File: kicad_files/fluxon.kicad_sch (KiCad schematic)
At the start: 159 parts, among them J1 Conn_ARM_JTAG_SWD_10, J2 U-F-M5DD-W-2, Q1 DTC123JKAT146, Q2 AO3402, SW1 ESC, SW10 O, SW11 P, SW12 DEL, SW13 BKSP, SW14 TAB_125, SW15 A, SW16 S, SW17 D, SW18 F, SW19 G, SW2 Q, SW20 H, SW21 J, SW22 K, SW23 L, SW24 QUOTE, SW25 ENTER_175, SW26 LSHIFT_175, SW27 Z, SW28 X, SW29 C, SW3 W, SW30 V, SW31 B, SW32 N, SW33 M, SW34 COMMA, SW35 DOT, SW36 RSHIFT_125, SW37 FN_100, SW38 RSHIFT_225, SW39 LCTRL_125, SW4 E, SW40 SUPER_100, SW41 LALT_100, SW42 SPC_625, SW43 RALT_125, SW44 RGUI_100, SW45 RCTRL_125, SW46 PN_100, SW47 SPC_175, SW48 SPC_275, SW49 FN_100, SW5 R, SW50 RALT_100, SW51 LCTRL_150, SW52 LALT_150, SW53 SPC_700, SW54 RCTRL_150, SW55 RALT_150, SW56 SW_Push, SW57 Rotary_Encoder_Switch_Chassis, SW6 T, SW7 Y, SW8 U, SW9 I, U1 USBLC6-2SC6, U2 STM32F072CBT6, U3 MCP1700-3302E/TT

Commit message: Add software reset circuit
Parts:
- removed C10: 4.7nF, Capacitor_SMD:C_0805_2012Metric, symbol Device:C_Small
- removed C11, C12: 100n, Capacitor_SMD:C_0805_2012Metric_Pad1.15x1.40mm_HandSolder, symbol Device:C_Small
- removed R13: 1M, acheron_Components:R_SMD_1206, symbol Device:R_Small
- removed R15, R16, R17, R18: 10k, acheron_Components:R_SMD_1206, symbol Device:R_Small
- removed SW57: Rotary_Encoder_Switch_Chassis, acheron_Hardware:ALPS_EC11E, symbol acheronSymbols:Rotary_Encoder_Switch_Chassis
- added Q3: DTA143EKAT146, Package_TO_SOT_SMD:SOT-23, symbol Transistor_BJT:DTA143E
- added R1: 100, acheron_Components:R_SMD_1206, symbol Device:R_Small
- added SW57: (I) RSHIFT_125, acheron_MX_SolderMask:MX125, symbol acheronSymbols:MXSwitch
- added SW58: BKSP_2U, acheron_MX_SolderMask:MX200, symbol acheronSymbols:MXSwitch
- added SW59: (I) SLASH_100, acheron_MX_SolderMask:MX100, symbol acheronSymbols:MXSwitch
- C10: renamed from CB2; value 100nF -> 100n
- C12: renamed from CB4; value 4.7uF -> 4.7u
- C13: renamed from CB5; value 1uF -> 1u
- C16: renamed from CB8; value 4.7uF -> 4.7u
- SW36: value RSHIFT_125 -> (D) RSHIFT_125
- SW37: value FN_100 -> (D) FN_100
- SW38: value RSHIFT_225 -> (F) RSHIFT_225
- renumbered CB1 to C1, CB3 to C11, CB6 to C14, CB7 to C15
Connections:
- net ROT_A is gone; now on net Col12: U2.42 (I2C1_SCL/PB6)
- net 3.3V: now also Q3.2 (E)
- net BOOT0: now also R1.2
- net Col11: now also SW59.1 (Col)
- net Col12: now also SW57.1 (Col), SW58.2 (Row); no longer U2.40 (SPI1_MISO/I2S1_MCK/TIM3_CH1/PB4)
- net at D36.2 (A), SW36.2 (Row), SW38.2 (Row): now also SW59.2 (Row)
- net at D37.2 (A), SW37.2 (Row): now also SW57.2 (Row)
- net M1: no longer names the net of D13.2 (A), SW13.1 (Col)
- net M1: now also SW58.1 (Col)
- net ROT_B renamed SOFT_RESET
- net SOFT_RESET: now also Q3.1 (B)
- new net: Q3.3 (C), R1.1
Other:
- note added: "(L) "Long" 6.25 bottom row"
- note removed: "(L) 6.25 bottom row"
- moved on the sheet: C2, C4, D49, Q1, R14, R3, R4, SW56

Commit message: Finish routing
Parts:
- removed Q1: DTC123JKAT146, Package_TO_SOT_SMD:SOT-23, symbol Transistor_BJT:DTC123J
- removed Q3: DTA143EKAT146, Package_TO_SOT_SMD:SOT-23, symbol Transistor_BJT:DTA143E
- added GR6: Warning Sign, acheron_Graphics:warning_sign_3.6x3.2mm, symbol Mechanical:MountingHole
- added J3: Conn_02x10, acheron_Connectors:PinHeader_2x8_P2.54mm_Vertical, symbol Connector_Generic:Conn_01x16
- added Q2: MUN5335DW1T1G, acheron_Components:SOT-363_SC-70-6, symbol acheronSymbols:MUN5335DW1T1G
- R8: renamed from R5; value 100K -> 100k
- R9: renamed from R6; value 100K -> 100k
- renumbered C9 to C1, C7 to C2, C8 to C3, C3 to C4, C2 to C7, C4 to C8, C1 to C9, D14 to D13, D15 to D14, D16 to D15, D17 to D16, D18 to D17, D19 to D18, D20 to D19, D21 to D20, D22 to D21, D23 to D22, D24 to D23, D25 to D24, D26 to D25, D27 to D26, D28 to D27, D29 to D28, D30 to D29, D31 to D30, D32 to D31, D33 to D32, D34 to D33, D35 to D34, D36 to D35, D37 to D36, D38 to D37, D39 to D38, D40 to D39, D41 to D40, D42 to D41, D43 to D42, D44 to D43, D13 to D44, D52 to D48, D53 to D49, D54 to D50, D50 to D51, D51 to D52, D49 to D53, Q2 to Q1, R9 to R1, R14 to R10, R1 to R11, R3 to R12, R4 to R13, R7 to R2, R8 to R3, R10 to R4, R11 to R5, R12 to R6, R2 to R7, SW14 to SW13, SW15 to SW14, SW16 to SW15, SW17 to SW16, SW18 to SW17, SW19 to SW18, SW20 to SW19, SW21 to SW20, SW22 to SW21, SW23 to SW22, SW24 to SW23, SW25 to SW24, SW26 to SW25, SW27 to SW26, SW28 to SW27, SW29 to SW28, SW30 to SW29, SW31 to SW30, SW32 to SW31, SW33 to SW32, SW34 to SW33, SW35 to SW34, SW36 to SW35, SW37 to SW36, SW38 to SW37, SW57 to SW38, SW59 to SW39, SW39 to SW40, SW40 to SW41, SW41 to SW42, SW42 to SW43, SW43 to SW44, SW44 to SW45, SW45 to SW46, SW13 to SW47, SW58 to SW48, SW46 to SW49, SW47 to SW50, SW48 to SW51, SW49 to SW52, SW50 to SW53, SW51 to SW54, SW52 to SW55, SW53 to SW56, SW54 to SW57, SW55 to SW58, SW56 to SW59, U3 to U2, U2 to U3
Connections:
- net 3.3V: now also J3.15 (Pin_15), Q2.4 (C)
- net 5V: now also R2.1; no longer R2.2
- net Col1: now also U3.25 (PB12)
- net Col12: now also U3.41 (SPI1_MOSI/I2S1_SD/TIM3_CH2/PB5); no longer U3.42 (I2C1_SCL/PB6)
- net GND: now also J3.16 (Pin_16), Q2.1 (C)
- net Row1: now also U3.38 (PA15)
- net Row2: now also U3.39 (SPI1_SCK/I2S1_CK/TIM2_CH2/PB3)
- net Row4: now also U3.42 (I2C1_SCL/PB6)
- net SOFT_RESET: now also U3.40 (SPI1_MISO/I2S1_MCK/TIM3_CH1/PB4), Q2.5 (B); no longer U3.41 (SPI1_MOSI/I2S1_SD/TIM3_CH2/PB5)
- net at D53.2 (A), SW59.2: now also Q2.2 (B)
- net at R10.1: now also Q2.6 (C)
- net EXTRA18: now reaches U3.13 (PA3/TIM15_CH2/ADC_IN3)
- net EXTRA18: now also J3.14 (Pin_14)
- net EXTRA17: now reaches U3.14 (PA4/TIM14_CH1/ADC_IN4)
- net EXTRA17: now also J3.13 (Pin_13)
- net EXTRA16: now reaches U3.15 (PA5/ADC_IN5/DAC_OUT2)
- net EXTRA16: now also J3.12 (Pin_12)
- net EXTRA15: now reaches U3.16 (PA6/ADC_IN6/TIM3_CH1/TIM16_CH1)
- net EXTRA15: now also J3.11 (Pin_11)
- net EXTRA14: now reaches U3.17 (PA7/TIM3_CH2/TIM14_CH1/ADC_IN7)
- net EXTRA14: now also J3.10 (Pin_10)
- net EXTRA13: now reaches U3.18 (PB0/TIM3_CH3/ADC_IN8)
- net EXTRA13: now also J3.9 (Pin_9)
- net EXTRA12: now reaches U3.19 (PB1/TIM3_CH4/TIM14_CH1/ADC_IN9)
- net EXTRA12: now also J3.8 (Pin_8)
- net EXTRA11: now reaches U3.20 (PB2)
- net EXTRA11: now also J3.7 (Pin_7)
- net EXTRA10: now reaches U3.21 (PB10/SPI2_SCK/I2C2_SCL/TIM2_CH3)
- net EXTRA10: now also J3.6 (Pin_6)
- net EXTRA9: now reaches U3.22 (PB11/TIM2_CH4/I2C2_SDA)
- net EXTRA9: now also J3.5 (Pin_5)
- net EXTRA8: now reaches U3.27 (SPI2_MISO/I2S2_MCK/I2C2_SDA/TIM15_CH1/PB14)
- net EXTRA8: now also J3.4 (Pin_4)
- net EXTRA5: now reaches U3.29 (TIM1_CH1/PA8)
- net EXTRA5: now also J3.3 (Pin_3)
- net EXTRA3: now reaches U3.30 (TIM1_CH2/PA9)
- net EXTRA3: now also J3.1 (Pin_1)
- net EXTRA6: now reaches U3.31 (TIM1_CH3/PA10)
- net EXTRA6: now also J3.2 (Pin_2)
- net at C2.2, D49.1 (VDD): now also R2.2; no longer R2.1
- net at R11.1: now also Q2.3 (C)
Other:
- note added: "RGB indicators"
- note removed: "REFERENCES"
- note removed: "[1] STM32F072x8 / STM32F072xB datasheet"
- note removed: "[2] AN4080 Application note"
- note removed: "https://www.st.com/content/ccc/resource/technical/document/application_note/c9/19/d7/b8/6b/0e/4c/d3/DM00051986.pdf/files/DM00051986.pdf/jcr:content/translations/en.DM00051986.pdf"
- note removed: "https://www.st.com/resource/en/datasheet/stm32f072rb.pdf"
- moved on the sheet: C1, C10, C11, C12, C13, C14, C15, C16, C2, C3, C4, C5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

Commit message: Quality of circuit improvements
- Adoption of STM32L072 MCU variant
- Changed TVS to SMF6.0A unidirectional
- Addition of regulation capacitor to voltage divider resistors in the level shifter circuit
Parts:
- added C17: 1u, Capacitor_SMD:C_0805_2012Metric_Pad1.15x1.40mm_HandSolder, symbol Device:C_Small
- D52: value SMF9.0CA -> SMF6.0A; footprint acheron_Components:D_SOD-123_Bidirectional -> acheron_Components:D_SOD-123; symbol Device:D_TVS -> Device:D_Schottky; LCSC Part Number C123799 -> C123790; Manufacturer Part Number SMF9.0CA -> SMF6.0A; Package SOD-123B -> SOD-123
- Q1: value AO3402 -> BSS138; LCSC Part Number C382313 -> C193019; Manufacturer KEXIN -> AnBom; Manufacturer Part Number AO3402 -> BSS138
- R4, R6: value 10k -> 1k
- R5: value 5.1k -> 510R
- U3: value STM32F072CBT6 -> STM32L072CBT6; LCSC Part Number C81720 -> C465977
- renumbered SW59 to S1
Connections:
- net 5V: now also C5.1, R5.2; no longer C5.2
- net GND: now also C5.2, C17.1; no longer C5.1
- net RGB_5V: no longer R5.2
- net at Q1.1 (G), R5.1, R6.2: now also C17.2
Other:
- title: HammerheadPCB -> Fluxon
- moved on the sheet: C5, Q1, R4, R5, R6, R8

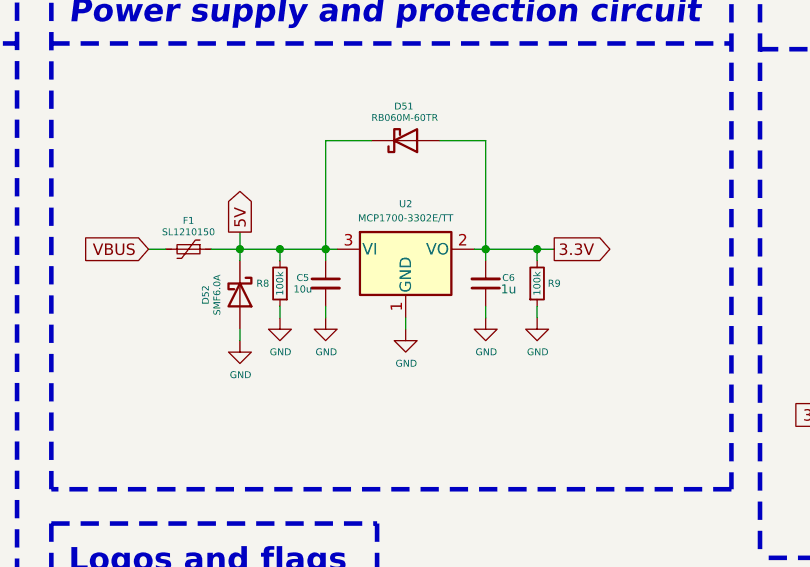
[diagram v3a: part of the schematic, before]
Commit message: Change LDO bypass capacitors to tantallum
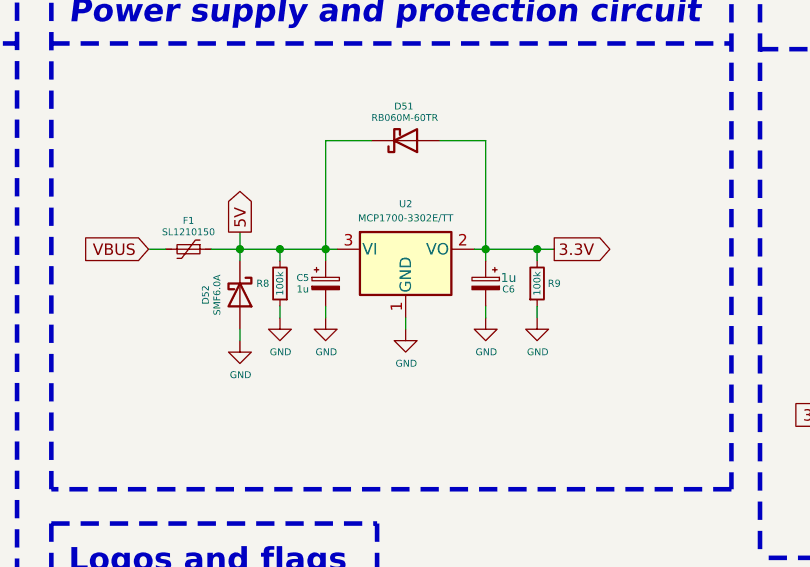
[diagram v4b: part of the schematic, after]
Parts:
- C5: value 10u -> 1u; footprint Capacitor_SMD:C_0805_2012Metric_Pad1.15x1.40mm_HandSolder -> acheron_Components:CP_EIA-3216-10_Kemet-I_Pad1.58x1.35mm_HandSolder; symbol Device:C_Small -> Device:CP_Small; Package C0805 -> CT3216
- C6: footprint Capacitor_SMD:C_0805_2012Metric_Pad1.15x1.40mm_HandSolder -> acheron_Components:CP_EIA-3216-10_Kemet-I_Pad1.58x1.35mm_HandSolder; symbol Device:C_Small -> Device:CP_Small; Package C0805 -> CT3216
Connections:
- net 3.3V: now also C6.1; no longer C6.2
- net GND: now also C6.2; no longer C6.1
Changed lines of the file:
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@@
   (junction (at 518.16 250.825) (diameter 0) (color 0 0 0 0))
   (junction (at 518.16 257.175) (diameter 0) (color 0 0 0 0))
+  (no_connect (at 127 271.145))
   (no_connect (at 64.77 347.345))
-  (no_connect (at 127 271.145))
   (no_connect (at 127 268.605))
   (no_connect (at 508.635 314.325))
@@
     )
   )
-  (symbol (lib_id "Device:C_Small") (at 51.435 363.855 180) (unit 1)
-    (in_bom yes) (on_board yes)
-    (property "Reference" "C4" (id 0) (at 47.625 363.855 90)
-      (effects (font (size 0.7874 0.7874)))
-    )
-    (property "Value" "4.7nF" (id 1) (at 48.895 363.855 90)
-      (effects (font (size 0.7874 0.7874)))
-    )
-    (property "Footprint" "Capacitor_SMD:C_0805_2012Metric" (id 2) (at 51.435 363.855 0)
-      (effects (font (size 1.27 1.27)) hide)
-    )
-    (property "Datasheet" "~" (id 3) (at 51.435 363.855 0)
-      (effects (font (size 1.27 1.27)) hide)
-    )
-    (property "Package" "C0805" (id 4) (at 51.435 363.855 0)
-      (effects (font (size 1.27 1.27)) hide)
-    )
-  )
-  (symbol (lib_id "Device:C_Small") (at 133.985 325.755 0) (unit 1)
+  (symbol (lib_id "Device:CP_Small") (at 133.985 325.755 0) (unit 1)
     (in_bom yes) (on_board yes)
     (property "Reference" "C5" (id 0) (at 131.445 325.12 0)
       (effects (font (size 0.762 0.762)))
     )
-    (property "Value" "10u" (id 1) (at 131.445 326.39 0)
-      (effects (font (size 0.7874 0.7874)))
-    )
-    (property "Footprint" "Capacitor_SMD:C_0805_2012Metric_Pad1.15x1.40mm_HandSolder" (id 2) (at 133.985 325.755 0)
+    (property "Value" "1u" (id 1) (at 131.445 326.39 0)
+      (effects (font (size 0.7874 0.7874)))
+    )
+    (property "Footprint" "acheron_Components:CP_EIA-3216-10_Kemet-I_Pad1.58x1.35mm_HandSolder" (id 2) (at 133.985 325.755 0)
       (effects (font (size 1.27 1.27)) hide)
     )
@@
       (effects (font (size 1.27 1.27)) hide)
     )
-    (property "Package" "C0805" (id 4) (at 133.985 325.755 0)
-      (effects (font (size 1.27 1.27)) hide)
-    )
-  )
-  (symbol (lib_id "Device:C_Small") (at 151.765 325.755 180) (unit 1)
-    (in_bom yes) (on_board yes)
-    (property "Reference" "C6" (id 0) (at 154.305 325.12 0)
+    (property "Package" "CT3216" (id 4) (at 133.985 325.755 0)
+      (effects (font (size 1.27 1.27)) hide)
+    )
+  )
+  (symbol (lib_id "Device:CP_Small") (at 151.765 325.755 0) (mirror y) (unit 1)
+    (in_bom yes) (on_board yes)
+    (property "Reference" "C6" (id 0) (at 154.305 326.39 0)
       (effects (font (size 0.762 0.762)))
     )
-    (property "Value" "1u" (id 1) (at 154.305 326.39 0)
+    (property "Value" "1u" (id 1) (at 154.305 325.12 0)
       (effects (font (size 0.9906 0.9906)))
     )
-    (property "Footprint" "Capacitor_SMD:C_0805_2012Metric_Pad1.15x1.40mm_HandSolder" (id 2) (at 151.765 325.755 0)
+    (property "Footprint" "acheron_Components:CP_EIA-3216-10_Kemet-I_Pad1.58x1.35mm_HandSolder" (id 2) (at 151.765 325.755 0)
       (effects (font (size 1.27 1.27)) hide)
     )
@@
       (effects (font (size 1.27 1.27)) hide)
     )
-    (property "Package" "C0805" (id 4) (at 151.765 325.755 0)
-      (effects (font (size 1.27 1.27)) hide)
-    )
+    (property "Package" "CT3216" (id 4) (at 151.765 325.755 0)
+      (effects (font (size 1.27 1.27)) hide)
+    )
+  )
+  (symbol (lib_id "Device:C_Small") (at 51.435 363.855 180) (unit 1)
+    (in_bom yes) (on_board yes)
+    (property "Reference" "C4" (id 0) (at 47.625 363.855 90)
+      (effects (font (size 0.7874 0.7874)))
+    )
+    (property "Value" "4.7nF" (id 1) (at 48.895 363.855 90)
+      (effects (font (size 0.7874 0.7874)))
+    )
+    (property "Footprint" "Capacitor_SMD:C_0805_2012Metric" (id 2) (at 51.435 363.855 0)
+      (effects (font (size 1.27 1.27)) hide)
+    )
+    (property "Datasheet" "~" (id 3) (at 51.435 363.855 0)
+      (effects (font (size 1.27 1.27)) hide)
+    )
+    (property "Package" "C0805" (id 4) (at 51.435 363.855 0)
+      (effects (font (size 1.27 1.27)) hide)
+    )

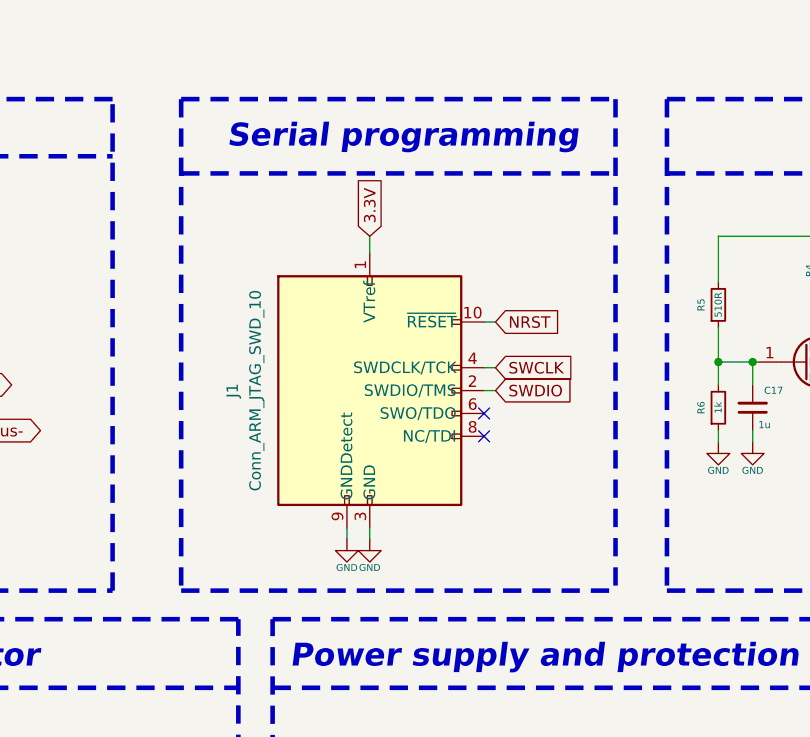
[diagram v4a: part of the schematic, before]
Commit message: Change ARM SWD JTAG to 6 pin variant
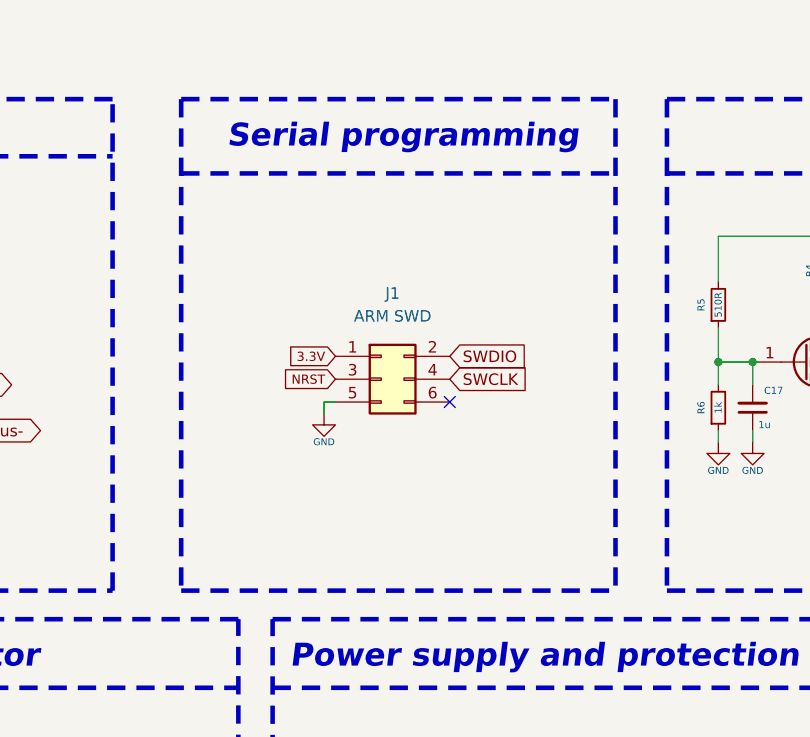
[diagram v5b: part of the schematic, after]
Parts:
- removed J1: Conn_ARM_JTAG_SWD_10, acheron_Connectors:Conn_ARM_JTAG_SWD_10, symbol Connector:Conn_ARM_JTAG_SWD_10
- added J1: ARM SWD, acheron_Connectors:Conn_ARM_JTAG_SWD_6, symbol Connector_Generic:Conn_02x03_Odd_Even
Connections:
- net 3.3V: now also J1.1 (Pin_1)
- net GND: now also J1.5 (Pin_5)
- net NRST: now also J1.3 (Pin_3)
- net SWCLK: now also J1.4 (Pin_4)
- net SWDIO: now also J1.2 (Pin_2)
- no-connect marks 4 -> 3
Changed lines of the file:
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@@
   (junction (at 518.16 250.825) (diameter 0) (color 0 0 0 0))
   (junction (at 518.16 257.175) (diameter 0) (color 0 0 0 0))
-  (no_connect (at 127 271.145))
   (no_connect (at 64.77 347.345))
-  (no_connect (at 127 268.605))
   (no_connect (at 508.635 314.325))
+  (no_connect (at 123.19 267.335))
   (wire (pts (xy 41.275 265.43) (xy 45.085 265.43))
     (stroke (width 0) (type solid) (color 0 0 0 0))
@@
     (stroke (width 0) (type solid) (color 0 0 0 0))
   )
-  (wire (pts (xy 111.76 282.575) (xy 111.76 281.305))
+  (wire (pts (xy 109.22 267.335) (xy 110.49 267.335))
+    (stroke (width 0) (type solid) (color 0 0 0 0))
+  )
+  (wire (pts (xy 109.22 268.605) (xy 109.22 267.335))
     (stroke (width 0) (type solid) (color 0 0 0 0))
   )
@@
     (stroke (width 0) (type solid) (color 0 0 0 0))
   )
-  (wire (pts (xy 114.3 248.92) (xy 114.3 250.825))
-    (stroke (width 0) (type solid) (color 0 0 0 0))
-  )
-  (wire (pts (xy 114.3 282.575) (xy 114.3 281.305))
-    (stroke (width 0) (type solid) (color 0 0 0 0))
-  )
   (wire (pts (xy 114.3 321.945) (xy 116.205 321.945))
     (stroke (width 0) (type solid) (color 0 0 0 0))
@@
     (stroke (width 0) (type solid) (color 0 0 0 0))
   )
-  (wire (pts (xy 128.27 258.445) (xy 127 258.445))
-    (stroke (width 0) (type solid) (color 0 0 0 0))
-  )
-  (wire (pts (xy 128.27 263.525) (xy 127 263.525))
-    (stroke (width 0) (type solid) (color 0 0 0 0))
-  )
-  (wire (pts (xy 128.27 266.065) (xy 127 266.065))
-    (stroke (width 0) (type solid) (color 0 0 0 0))
-  )
   (wire (pts (xy 128.905 321.945) (xy 128.905 323.215))
     (stroke (width 0) (type solid) (color 0 0 0 0))
@@
     (effects (font (size 1.27 1.27)) (justify left))
   )
-  (global_label "Col2" (shape input) (at 112.395 28.575 90)
-    (effects (font (size 1.27 1.27)) (justify left))
+  (global_label "3.3V" (shape input) (at 110.49 262.255 180)
+    (effects (font (size 1.016 1.016)) (justify right))
   )
-  (global_label "3.3V" (shape input) (at 114.3 248.92 90)
+  (global_label "NRST" (shape input) (at 110.49 264.795 180)
+    (effects (font (size 1.016 1.016)) (justify right))
+  )
+  (global_label "Col2" (shape input) (at 112.395 28.575 90)
     (effects (font (size 1.27 1.27)) (justify left))
   )
@@
     (effects (font (size 1.27 1.27)) (justify right))
   )
-  (global_label "5V" (shape output) (at 124.46 320.04 90)
-    (effects (font (size 1.27 1.27)) (justify left))
-  )
-  (global_label "NRST" (shape input) (at 128.27 258.445 0)
+  (global_label "SWDIO" (shape input) (at 123.19 262.255 0)
     (effects (font (size 1.27 1.27)) (justify left))
   )
-  (global_label "SWCLK" (shape input) (at 128.27 263.525 0)
+  (global_label "SWCLK" (shape input) (at 123.19 264.795 0)
     (effects (font (size 1.27 1.27)) (justify left))
   )
-  (global_label "SWDIO" (shape input) (at 128.27 266.065 0)
+  (global_label "5V" (shape output) (at 124.46 320.04 90)
     (effects (font (size 1.27 1.27)) (justify left))
   )
@@
     )
   )
-  (symbol (lib_id "power:GND") (at 111.76 282.575 0) (mirror y) (unit 1)
-    (in_bom yes) (on_board yes)
-    (property "Reference" "#PWR09" (id 0) (at 111.76 288.925 0)
-      (effects (font (size 1.27 1.27)) hide)
-    )
-    (property "Value" "GND" (id 1) (at 111.76 285.75 0)
-      (effects (font (size 0.762 0.762)))
-    )
-    (property "Footprint" "" (id 2) (at 111.76 282.575 0)
-      (effects (font (size 1.27 1.27)) hide)
-    )
-    (property "Datasheet" "" (id 3) (at 111.76 282.575 0)
-      (effects (font (size 1.27 1.27)) hide)
-    )
-  )
-  (symbol (lib_id "power:GND") (at 114.3 282.575 0) (mirror y) (unit 1)
+  (symbol (lib_id "power:GND") (at 109.22 268.605 0) (mirror y) (unit 1)
     (in_bom yes) (on_board yes)
-    (property "Reference" "#PWR010" (id 0) (at 114.3 288.925 0)
+    (property "Reference" "#PWR?" (id 0) (at 109.22 274.955 0)
       (effects (font (size 1.27 1.27)) hide)
     )
-    (property "Value" "GND" (id 1) (at 114.3 285.75 0)
+    (property "Value" "GND" (id 1) (at 109.22 271.78 0)
       (effects (font (size 0.762 0.762)))
     )
-    (property "Footprint" "" (id 2) (at 114.3 282.575 0)
+    (property "Footprint" "" (id 2) (at 109.22 268.605 0)
       (effects (font (size 1.27 1.27)) hide)
     )
-    (property "Datasheet" "" (id 3) (at 114.3 282.575 0)
+    (property "Datasheet" "" (id 3) (at 109.22 268.605 0)
       (effects (font (size 1.27 1.27)) hide)
     )
@@
     )
   )
+  (symbol (lib_id "Connector_Generic:Conn_02x03_Odd_Even") (at 115.57 264.795 0) (unit 1)
+    (in_bom no) (on_board yes)
+    (property "Reference" "J1" (id 0) (at 116.84 255.27 0))
+    (property "Value" "ARM SWD" (id 1) (at 116.84 257.81 0))
+    (property "Footprint" "acheron_Connectors:Conn_ARM_JTAG_SWD_6" (id 2) (at 115.57 264.795 0)
+      (effects (font (size 1.27 1.27)) hide)
+    )
+    (property "Datasheet" "~" (id 3) (at 115.57 264.795 0)
+      (effects (font (size 1.27 1.27)) hide)
+    )
+  )
   (symbol (lib_id "Device:Q_NMOS_GSD") (at 162.56 262.89 0) (unit 1)
     (in_bom yes) (on_board yes)
@@
     )
   )
-  (symbol (lib_id "Connector:Conn_ARM_JTAG_SWD_10") (at 114.3 266.065 0) (unit 1)
-    (in_bom yes) (on_board yes)
-    (property "Reference" "J1" (id 0) (at 99.06 266.065 90))
-    (property "Value" "Conn_ARM_JTAG_SWD_10" (id 1) (at 101.6 266.065 90))
-    (property "Footprint" "acheron_Connectors:Conn_ARM_JTAG_SWD_10" (id 2) (at 114.3 266.065 0)
-      (effects (font (size 1.27 1.27)) hide)
-    )
-    (property "Datasheet" "http://infocenter.arm.com/help/topic/com.arm.doc.ddi0314h/DDI0314H_coresight_components_trm.pdf" (id 3) (at 105.41 297.815 90)
-      (effects (font (size 1.27 1.27)) hide)
-    )
-  )
   (symbol (lib_id "acheronSymbols:STM32F072-LQFP48") (at 462.28 285.115 0) (unit 1)
     (in_bom yes) (on_board yes)
@@
       (reference "#PWR08") (unit 1)
     )
-    (path "/00000000-0000-0000-0000-00005d9bcef9"
-      (reference "#PWR09") (unit 1)
-    )
-    (path "/00000000-0000-0000-0000-00005cfdfc6d"
-      (reference "#PWR010") (unit 1)
-    )
     (path "/00000000-0000-0000-0000-00005d7660d9"
       (reference "#PWR011") (unit 1)
@@
       (reference "#PWR0102") (unit 1)
     )
+    (path "/c38fbb2a-c35b-4672-8fd1-d78ffb85c184"
+      (reference "#PWR?") (unit 1)
+    )
     (path "/d5072c79-7bfb-447b-9669-32e9fefbcb51"
       (reference "C1") (unit 1)
@@
       (reference "GR6") (unit 1)
     )
-    (path "/00000000-0000-0000-0000-00005d896ff6"
+    (path "/3bf1228b-aee4-4155-9b64-00626b023658"
       (reference "J1") (unit 1)
     )
